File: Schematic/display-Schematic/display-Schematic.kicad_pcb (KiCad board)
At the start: 2 copper layers, 190 x 45 mm, 36 parts, among them SW1 up, SW2 left, SW3 left, SW4 down, SW5 setup, U10 5161AS, U11 5161AS, U12 5161AS, U13 5161AS, U4 MAX7219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

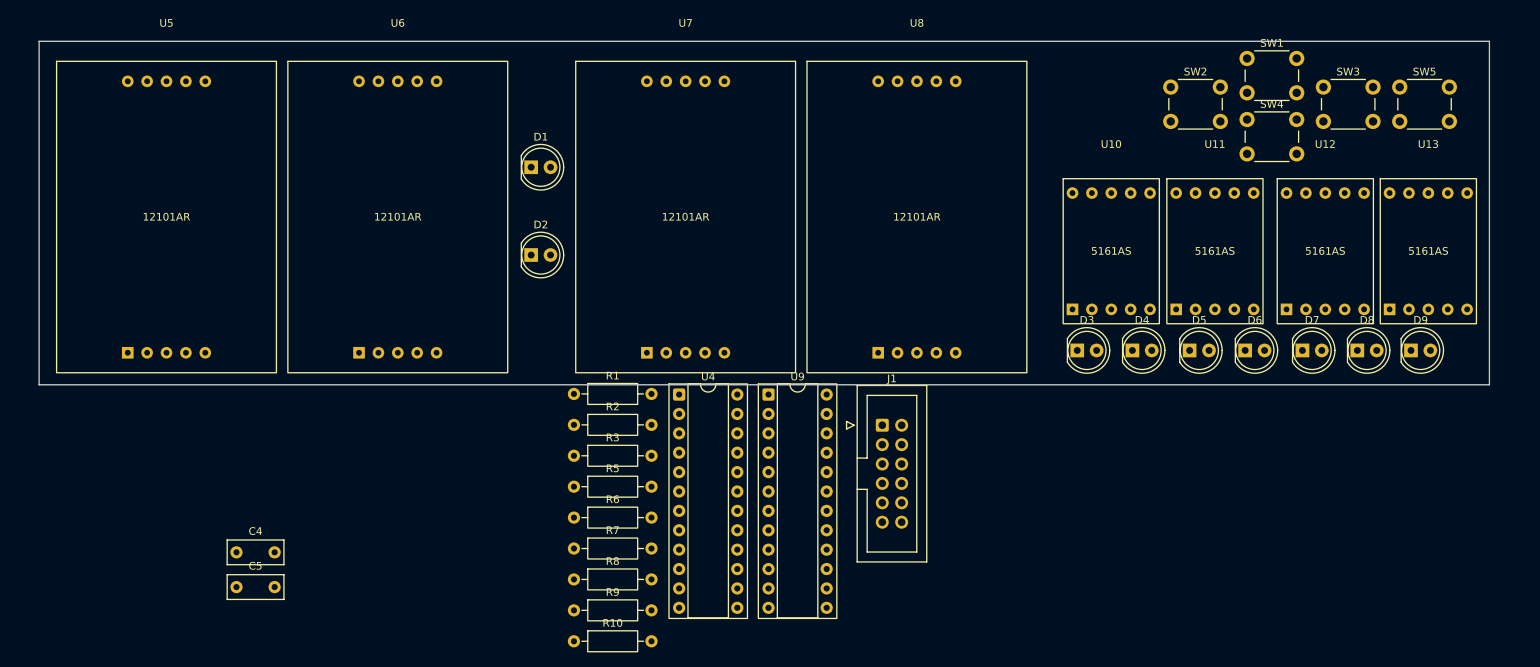
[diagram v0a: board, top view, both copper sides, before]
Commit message: started the rooting but some thing moved and now every thing is miss placed I must start from the beginning again
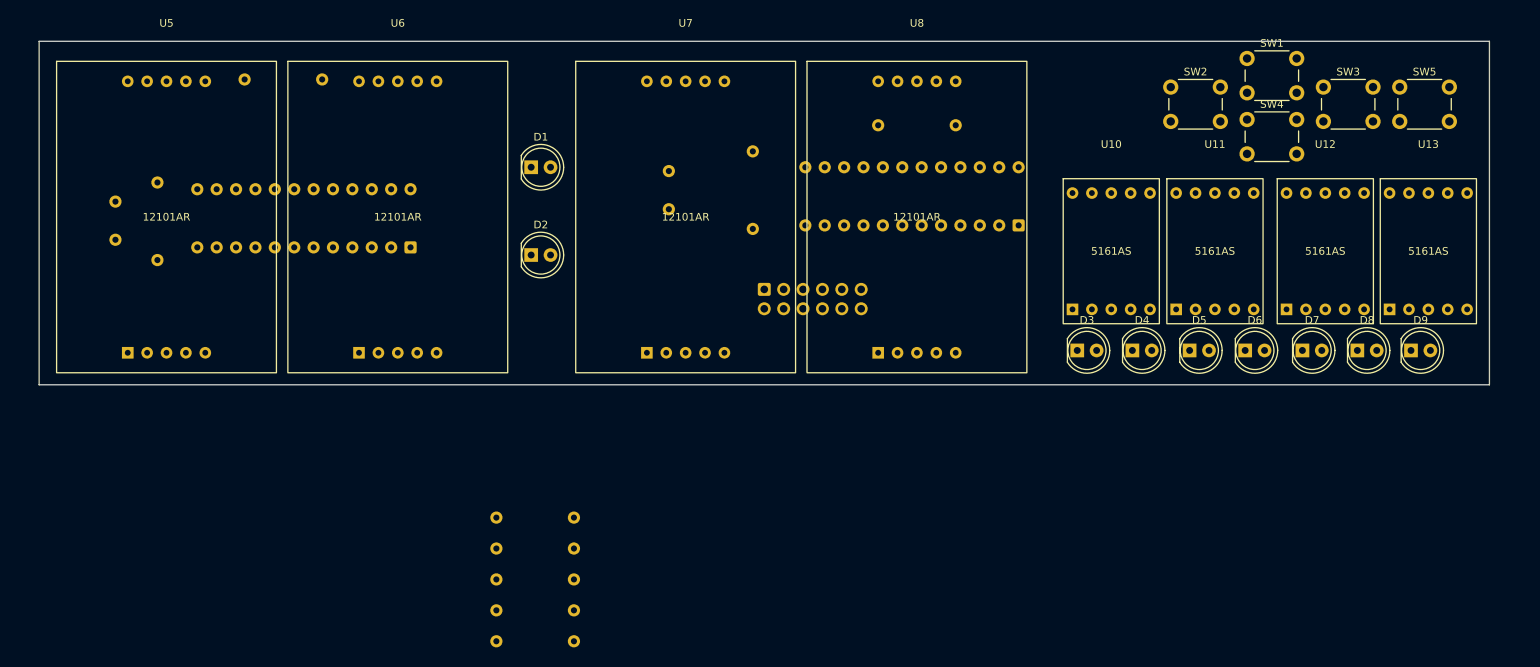
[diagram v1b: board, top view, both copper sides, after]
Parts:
- C4, C5, J1, R1, R10, R2, R3, R5, R6, R7, R8, R9, U4, U9: moved to B.Cu
- moved C5 78.6 mm to (137.5, 94.5), turned to -90 degrees
- moved R5 68.9 mm to (175.1, 88.5), turned to 180 degrees
- moved R2 63.1 mm to (70.5, 96.0), turned to -90 degrees
- moved R3 59.3 mm to (92.1, 82.5), turned to 180 degrees
- moved C4 48.6 mm to (65.0, 98.5), turned to -90 degrees
- moved U4 40.1 mm to (103.7, 104.5), turned to 90 degrees
- moved U9 39.6 mm to (183.3, 101.6), turned to 90 degrees
- moved R1 39.5 mm to (148.5, 91.9), turned to -90 degrees
- moved J1 23.6 mm to (150.0, 110.0), turned to -90 degrees
- turned R10 to 180 degrees
- turned R6 to 180 degrees
- turned R7 to 180 degrees
- turned R8 to 180 degrees
- turned R9 to 180 degrees

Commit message: Finished the display PCB. A lot of changes went throough to ensure only one layer was used for connections. To change : plug pin placement ; switches are now pull up ; in the code : digit codes are now differents, and differents from display 1 to display 2
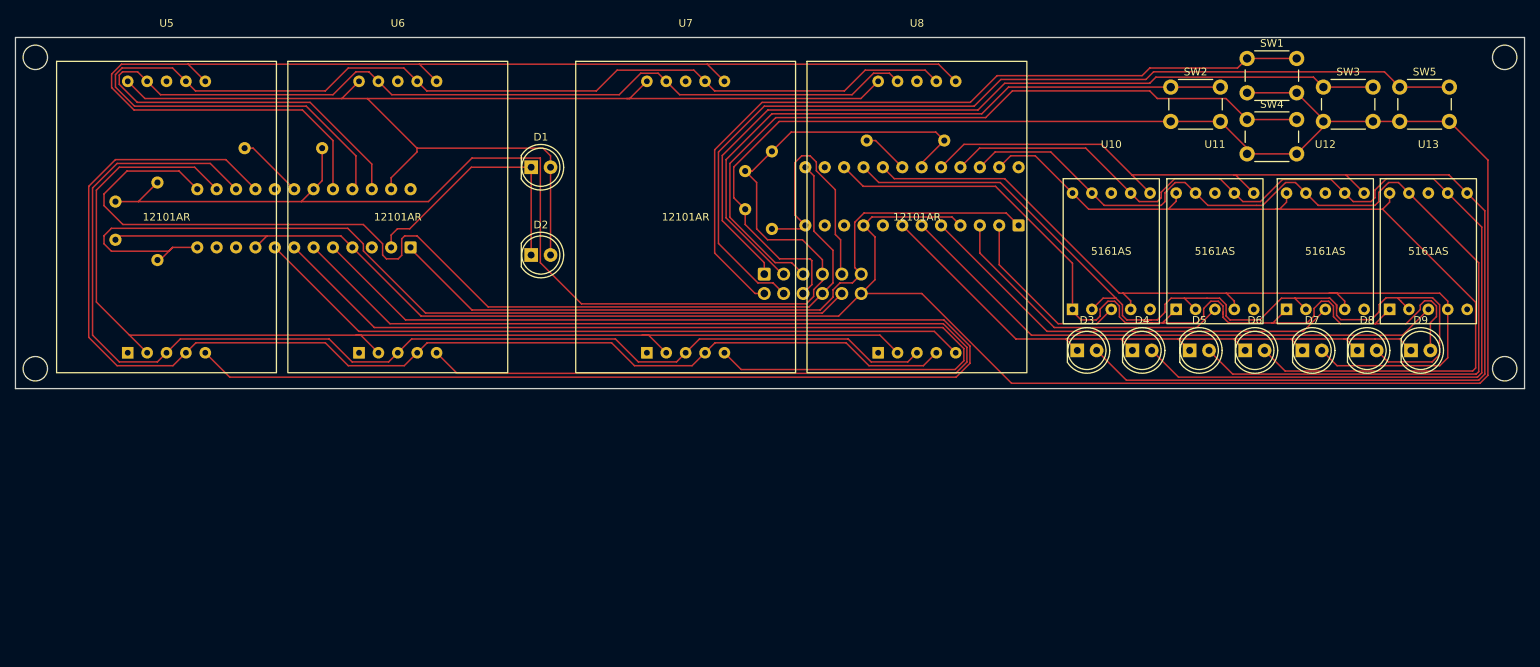
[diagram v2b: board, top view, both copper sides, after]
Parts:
- removed R10, R6, R7, R8, R9: 10k, Resistor_THT:R_Axial_DIN0207_L6.3mm_D2.5mm_P10.16mm_Horizontal
- U4, U9: footprint Package_DIP:CERDIP-24_W7.62mm_SideBrazed_Socket -> Package_DIP:DIP-24_W7.62mm
- moved C5 10.0 mm to (147.5, 94.5)
- moved R3 9.00 mm to (92.1, 91.5)
- moved R1 2.50 mm to (151.0, 91.9)
- moved R5 2.50 mm to (173.6, 90.5)
- moved J1 2.00 mm to (150.0, 108.0)
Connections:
- J1 pad 1: Net-(U4-LOAD) -> Net-(SW3A-C)
- J1 pad 10: +5V -> Net-(U4-LOAD)
- J1 pad 11: +3.3V -> Net-(U4-DIN)
- J1 pad 2: Net-(U4-CLK) -> Net-(SW1A-C)
- J1 pad 3: Net-(U4-DIN) -> Net-(SW2A-C)
- J1 pad 4: Net-(U9-LOAD) -> Net-(SW5A-C)
- J1 pad 5: Net-(SW5A-C) -> Net-(SW4A-C)
- J1 pad 6: Net-(SW3A-C) -> GND
- J1 pad 7: Net-(SW2A-C) -> +5V
- J1 pad 8: Net-(SW1A-C) -> Net-(U4-CLK)
- J1 pad 9: Net-(SW4A-C) -> Net-(U9-LOAD)
- SW1 pad 2: +3.3V -> GND
- SW2 pad 2: +3.3V -> GND
- SW3 pad 2: +3.3V -> GND
- SW4 pad 2: +3.3V -> GND
- SW5 pad 2: +3.3V -> GND
- U10 pad 1: Net-(D7-A) -> Net-(D9-A)
- U10 pad 10: Net-(D9-A) -> Net-(D6-A)
- U10 pad 2: Net-(D6-A) -> Net-(D8-A)
- U10 pad 4: Net-(D5-A) -> Net-(D7-A)
- U10 pad 6: Net-(D4-A) -> Net-(D3-A)
- U10 pad 7: Net-(D3-A) -> Net-(D4-A)
- U10 pad 9: Net-(D8-A) -> Net-(D5-A)
- U11 pad 1: Net-(D7-A) -> Net-(D9-A)
- U11 pad 10: Net-(D9-A) -> Net-(D6-A)
- U11 pad 2: Net-(D6-A) -> Net-(D8-A)
- U11 pad 3: Net-(U9-DIG_1) -> Net-(U9-DIG_4)
- U11 pad 4: Net-(D5-A) -> Net-(D7-A)
- U11 pad 6: Net-(D4-A) -> Net-(D3-A)
- U11 pad 7: Net-(D3-A) -> Net-(D4-A)
- U11 pad 9: Net-(D8-A) -> Net-(D5-A)
- U12 pad 1: Net-(D7-A) -> Net-(D9-A)
- U12 pad 10: Net-(D9-A) -> Net-(D6-A)
- U12 pad 2: Net-(D6-A) -> Net-(D8-A)
- U12 pad 3: Net-(U9-DIG_2) -> Net-(U9-DIG_6)
- U12 pad 4: Net-(D5-A) -> Net-(D7-A)
- U12 pad 6: Net-(D4-A) -> Net-(D3-A)
- U12 pad 7: Net-(D3-A) -> Net-(D4-A)
- U12 pad 9: Net-(D8-A) -> Net-(D5-A)
- U13 pad 1: Net-(D7-A) -> Net-(D9-A)
- U13 pad 10: Net-(D9-A) -> Net-(D6-A)
- U13 pad 2: Net-(D6-A) -> Net-(D8-A)
- U13 pad 3: Net-(U9-DIG_3) -> Net-(U9-DIG_2)
- U13 pad 4: Net-(D5-A) -> Net-(D7-A)
- U13 pad 6: Net-(D4-A) -> Net-(D3-A)
- U13 pad 7: Net-(D3-A) -> Net-(D4-A)
- U13 pad 9: Net-(D8-A) -> Net-(D5-A)
- U4 pad 11: Net-(U4-DIG_1) -> unconnected-(U4-DIG_1-Pad11)
- U4 pad 14: Net-(D1-A) -> Net-(U4-SEG_A)
- U4 pad 17: Net-(U4-SEG_G) -> unconnected-(U4-SEG_G-Pad17)
- U4 pad 2: Net-(U4-DIG_0) -> Net-(D1-K)
- U4 pad 22: unconnected-(U4-SEG_DP-Pad22) -> Net-(U4-SEG_DP)
- U4 pad 23: Net-(U4-SEG_D) -> Net-(D1-A)
- U4 pad 3: Net-(D1-K) -> unconnected-(U4-DIG_4-Pad3)
- U4 pad 5: unconnected-(U4-DIG_6-Pad5) -> Net-(U4-DIG_6)
- U4 pad 8: unconnected-(U4-DIG_7-Pad8) -> Net-(U4-DIG_7)
- U5 pad 10: Net-(U4-SEG_G) -> Net-(D1-A)
- U5 pad 2: Net-(U4-SEG_E) -> Net-(U4-SEG_A)
- U5 pad 3: Net-(U4-SEG_D) -> Net-(U4-SEG_F)
- U5 pad 4: Net-(U4-SEG_C) -> Net-(U4-SEG_B)
- U5 pad 5: Net-(U4-DIG_0) -> Net-(U4-DIG_6)
- U5 pad 6: Net-(U4-SEG_B) -> Net-(U4-SEG_C)
- U5 pad 7: Net-(D1-A) -> Net-(U4-SEG_E)
- U5 pad 9: Net-(U4-SEG_F) -> Net-(U4-SEG_DP)
- U6 pad 10: Net-(U4-SEG_G) -> Net-(D1-A)
- U6 pad 2: Net-(U4-SEG_E) -> Net-(U4-SEG_A)
- U6 pad 3: Net-(U4-SEG_D) -> Net-(U4-SEG_F)
- U6 pad 4: Net-(U4-SEG_C) -> Net-(U4-SEG_B)
- U6 pad 5: Net-(U4-DIG_1) -> Net-(U4-DIG_2)
- U6 pad 6: Net-(U4-SEG_B) -> Net-(U4-SEG_C)
- U6 pad 7: Net-(D1-A) -> Net-(U4-SEG_E)
- U6 pad 9: Net-(U4-SEG_F) -> Net-(U4-SEG_DP)
- U7 pad 10: Net-(U4-SEG_G) -> Net-(D1-A)
- U7 pad 2: Net-(U4-SEG_E) -> Net-(U4-SEG_A)
- U7 pad 3: Net-(U4-SEG_D) -> Net-(U4-SEG_F)
- U7 pad 4: Net-(U4-SEG_C) -> Net-(U4-SEG_B)
- U7 pad 5: Net-(U4-DIG_2) -> Net-(U4-DIG_3)
- U7 pad 6: Net-(U4-SEG_B) -> Net-(U4-SEG_C)
- U7 pad 7: Net-(D1-A) -> Net-(U4-SEG_E)
- U7 pad 9: Net-(U4-SEG_F) -> Net-(U4-SEG_DP)
- U8 pad 10: Net-(U4-SEG_G) -> Net-(D1-A)
- U8 pad 2: Net-(U4-SEG_E) -> Net-(U4-SEG_A)
- U8 pad 3: Net-(U4-SEG_D) -> Net-(U4-SEG_F)
- U8 pad 4: Net-(U4-SEG_C) -> Net-(U4-SEG_B)
- U8 pad 5: Net-(U4-DIG_3) -> Net-(U4-DIG_7)
- U8 pad 6: Net-(U4-SEG_B) -> Net-(U4-SEG_C)
- U8 pad 7: Net-(D1-A) -> Net-(U4-SEG_E)
- U8 pad 9: Net-(U4-SEG_F) -> Net-(U4-SEG_DP)
- U9 pad 11: Net-(U9-DIG_1) -> unconnected-(U9-DIG_1-Pad11)
- U9 pad 14: Net-(D3-A) -> unconnected-(U9-SEG_A-Pad14)
- U9 pad 15: Net-(D8-A) -> Net-(D9-A)
- U9 pad 16: Net-(D4-A) -> Net-(D8-A)
- U9 pad 17: Net-(D9-A) -> Net-(D7-A)
- U9 pad 20: Net-(D5-A) -> Net-(D3-A)
- U9 pad 21: Net-(D7-A) -> Net-(D4-A)
- U9 pad 22: unconnected-(U9-SEG_DP-Pad22) -> Net-(D5-A)
- U9 pad 3: Net-(D3-K) -> Net-(U9-DIG_4)
- U9 pad 5: unconnected-(U9-DIG_6-Pad5) -> Net-(U9-DIG_6)
- U9 pad 7: Net-(U9-DIG_3) -> Net-(D3-K)
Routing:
- net GND: track 0.00 -> 389.0 mm
- net Net-(U4-DIG_6): track 0.00 -> 193.3 mm
- net +5V: track 0.00 -> 179.0 mm
- net Net-(U4-SEG_B): track 0.00 -> 165.4 mm
- net Net-(U4-DIG_2): track 0.00 -> 164.1 mm
- net Net-(U4-SEG_C): track 0.00 -> 161.6 mm
- net Net-(D3-A): track 0.00 -> 160.6 mm
- net Net-(U4-SEG_F): track 0.00 -> 158.2 mm
- net Net-(U4-SEG_E): track 0.00 -> 157.0 mm
- net Net-(D1-A): track 0.00 -> 154.2 mm
- net Net-(U4-SEG_A): track 0.00 -> 151.8 mm
- net Net-(U4-SEG_DP): track 0.00 -> 151.7 mm
- net Net-(D4-A): track 0.00 -> 146.0 mm
- net Net-(U4-CLK): track 0.00 -> 139.5 mm
- net Net-(D5-A): track 0.00 -> 132.0 mm
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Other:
- board size 190 x 45 mm -> 197.7 x 46 mm
- board text added: "${REFERENCE}"

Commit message: Further work on the hardware side of the pcb
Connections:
- J1 pad 6: GND -> +3.3V
- SW1 pad 2: GND -> +3.3V
- SW2 pad 2: GND -> +3.3V
- SW3 pad 2: GND -> +3.3V
- SW4 pad 2: GND -> +3.3V
- SW5 pad 2: GND -> +3.3V
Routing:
- net +3.3V: track 0.00 -> 138.0 mm
- net GND: track 389.0 -> 351.4 mm
- net Net-(SW1A-C): track 103.4 -> 104.6 mm
- net Net-(SW5A-C): track 124.2 -> 125.2 mm
- net Net-(SW4A-C): track 99.5 -> 100.5 mm
- net Net-(SW2A-C): track 86.9 -> 87.9 mm
- net Net-(SW3A-C): track 107.9 -> 108.8 mm

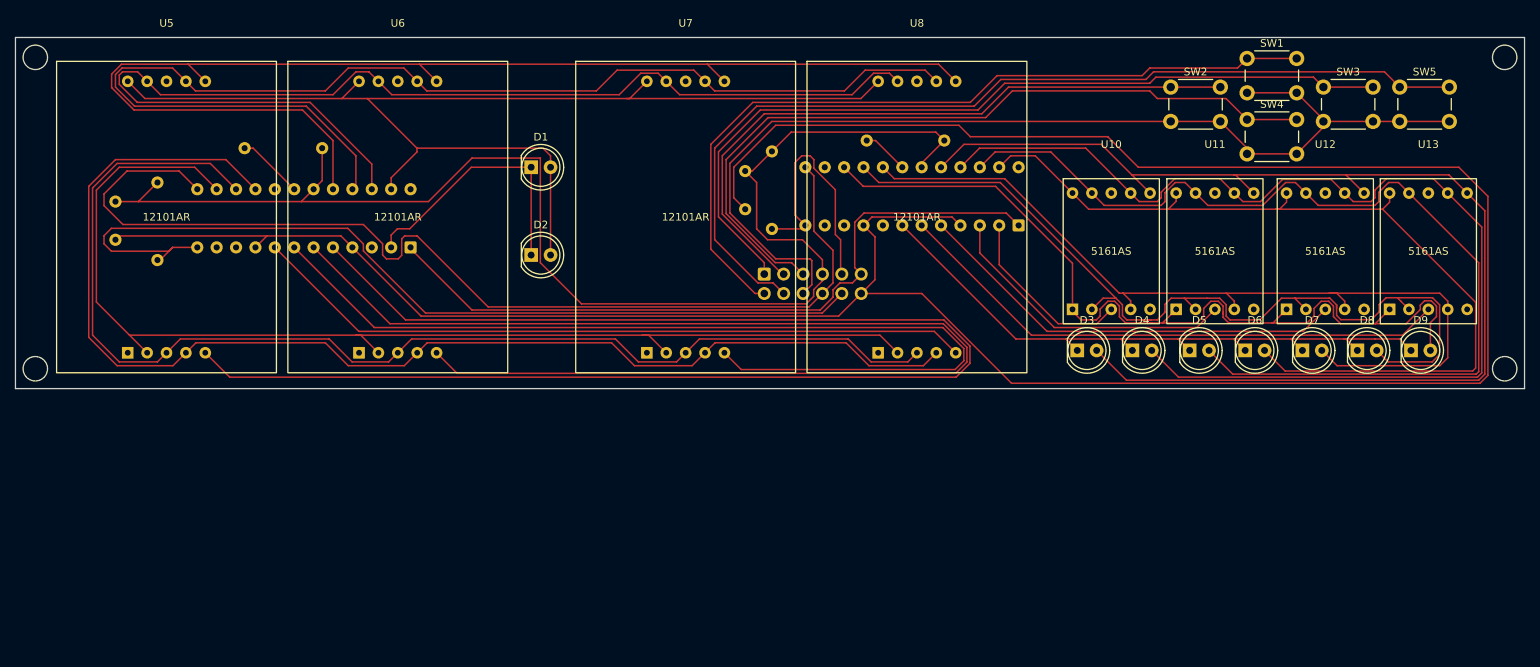
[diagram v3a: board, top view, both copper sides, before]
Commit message: Finished the PCBs. I had to use two jumper cable. I also adjusted the position of some traces close to pins
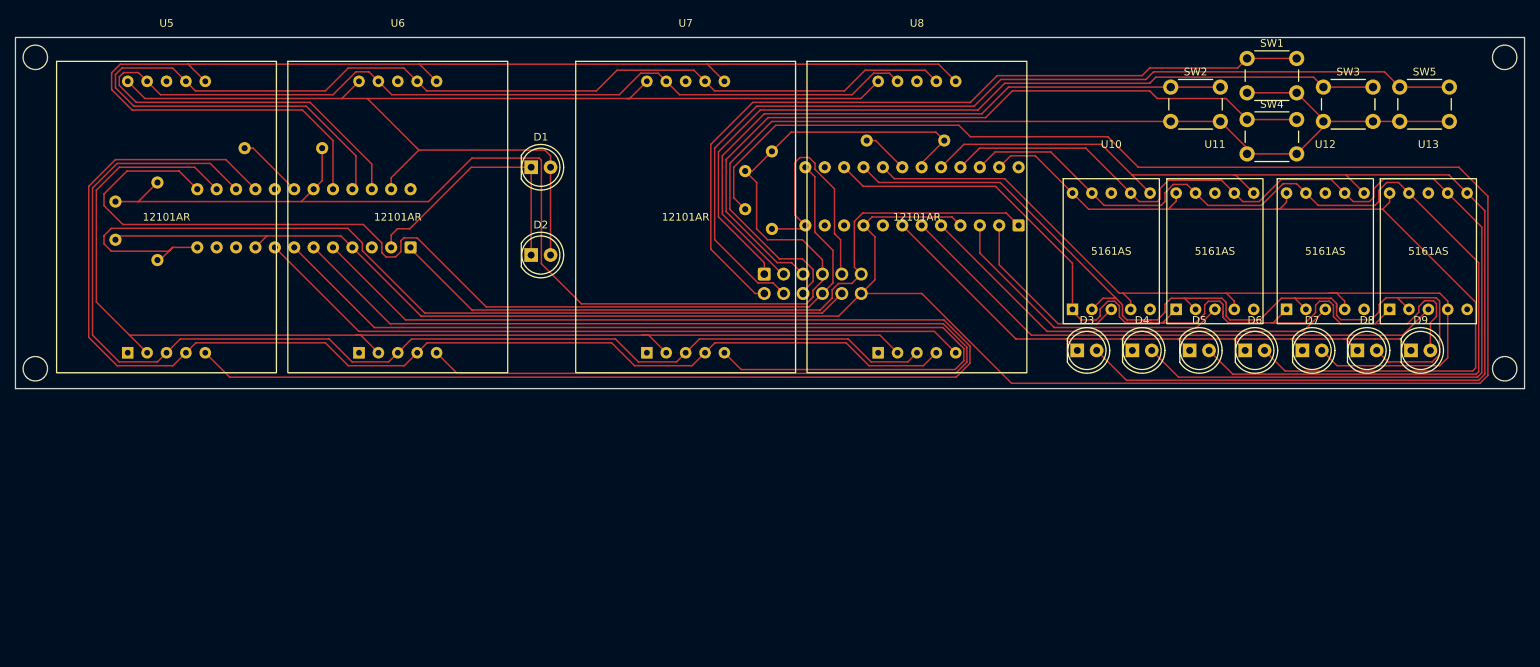
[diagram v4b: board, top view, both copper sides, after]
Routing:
- net Net-(U4-CLK): track 139.5 -> 138.6 mm
- net +3.3V: track 138.0 -> 137.3 mm
- net Net-(D8-A): track 121.3 -> 121.8 mm
- net Net-(D9-A): track 117.6 -> 118.1 mm
